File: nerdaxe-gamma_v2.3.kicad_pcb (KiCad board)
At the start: 4 copper layers, 60.8 x 99.8 mm, 130 parts, among them J1 54-00164, J6 Conn_01x04, T1 net-tie, U10 EMC2101, U11 T-Display-S3, U2 TPS546D24ARVFR, U5 MCP1824T-1202E/OT, U6 MCP1824T-0802E, U7 25MHz, U8 BM1370_mode1, U9 SN74AVC4T774

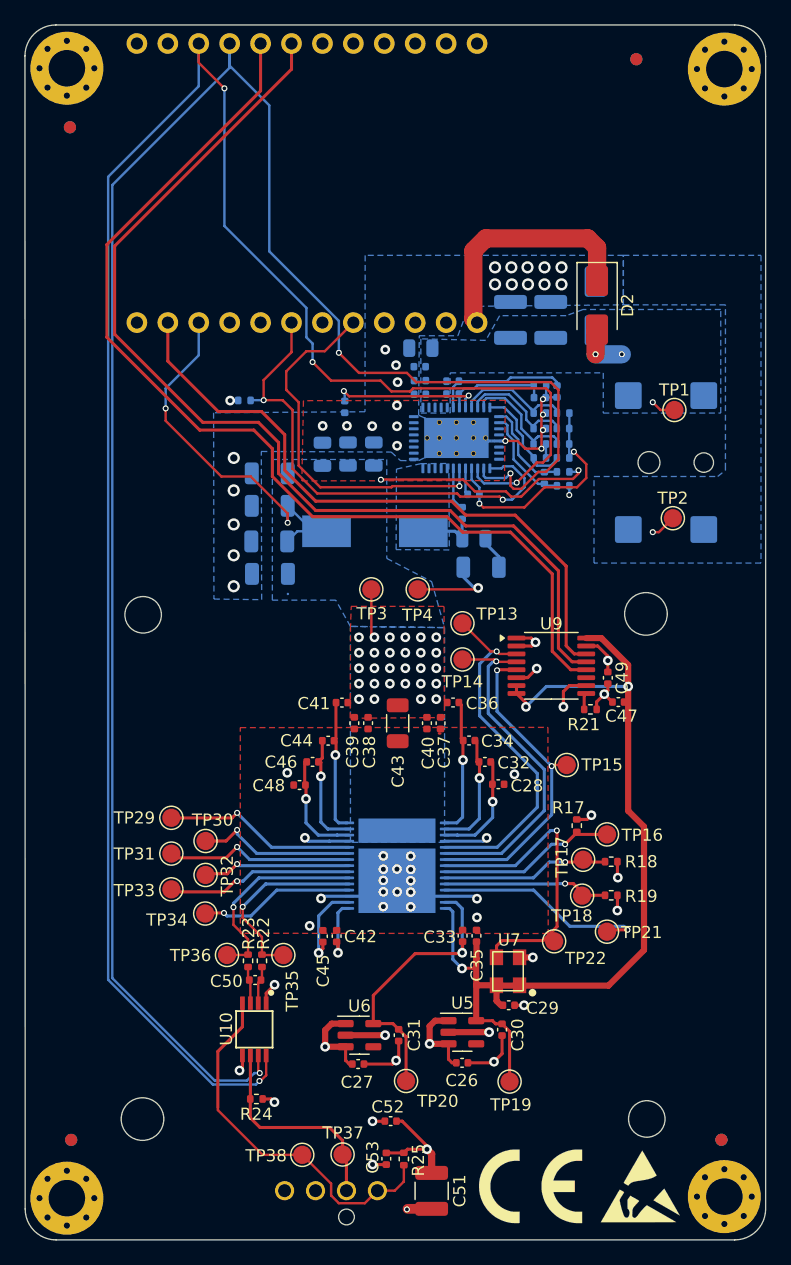
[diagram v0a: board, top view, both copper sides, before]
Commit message: Nerdaxe Gamma v2.3
- Fix Emi CE needs
- Added ferrite beads + EMI blocking capacitors
- New components added: R16, R20, R26, R27C21, C22, C23, FB1, FB2, FB3, FB4, FB5, FB6
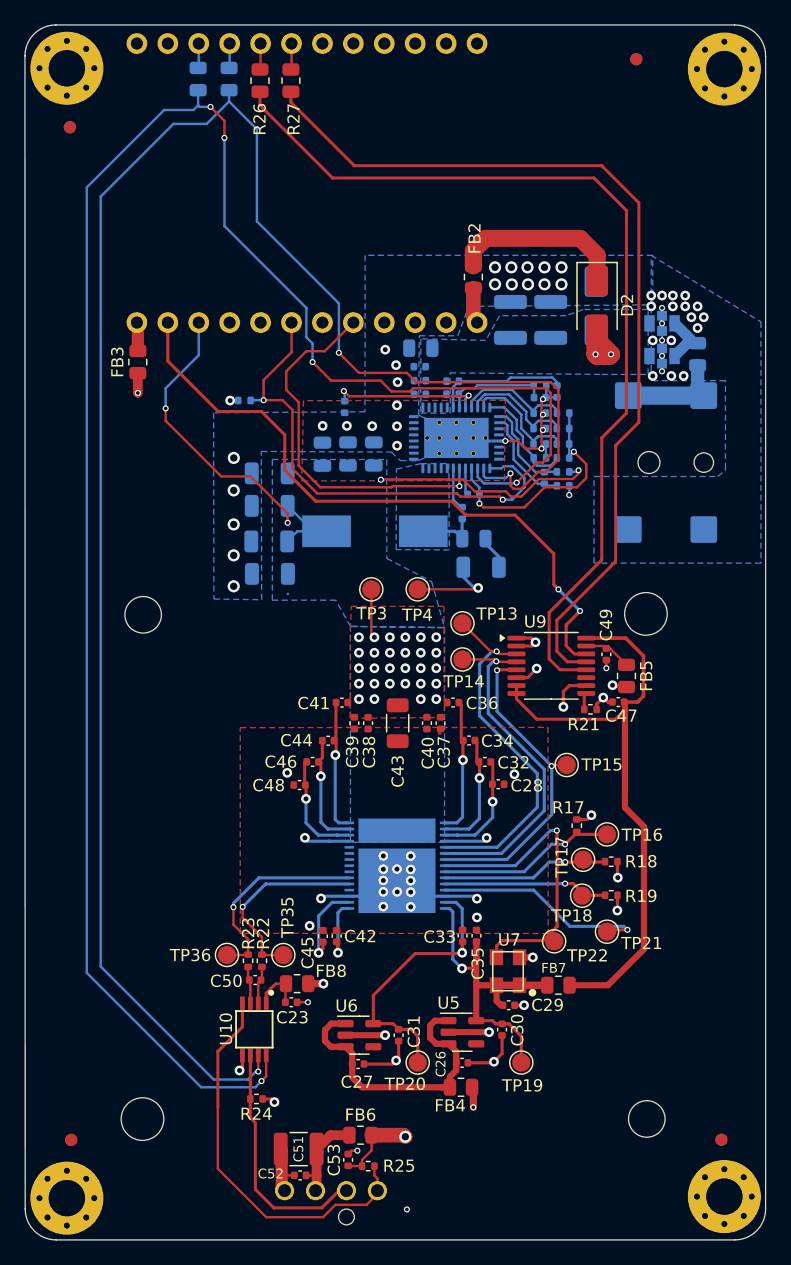
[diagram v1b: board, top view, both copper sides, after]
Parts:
- removed REF**: CE-Logo_8.5x6mm_SilkScreen, Symbol:CE-Logo_8.5x6mm_SilkScreen
- removed REF**: ESD-Logo_6.6x6mm_SilkScreen, Symbol:ESD-Logo_6.6x6mm_SilkScreen
- removed REF**: OSHW-Logo2_7.3x6mm_SilkScreen, Symbol:OSHW-Logo2_7.3x6mm_SilkScreen
- removed TP1, TP2, TP29, TP30, TP31, TP32, TP33, TP34, TP37, TP38: TestPoint, TestPoint:TestPoint_Pad_D1.5mm
- added C21: NFM21PC105B1C3D, bitaxe:NFM21PC105B1C3D_MUR, B.Cu at (127.4, 74.7)
- added C22: NFM21PC105B1C3D, bitaxe:NFM21PC105B1C3D_MUR, B.Cu at (127.4, 72.0)
- added C23: 0.1uF, Capacitor_SMD:C_0402_1005Metric, F.Cu at (96.9, 127.8)
- added FB1: 2508051217Y6, Resistor_SMD:R_0805_2012Metric, B.Cu at (130.3, 74.5)
- added FB2: MPZ2012S221A, Resistor_SMD:R_0805_2012Metric, F.Cu at (111.9, 68.2)
- added FB3: BLM21PG221SN1D, Resistor_SMD:R_0805_2012Metric, F.Cu at (84.3, 75.2)
- added FB4: BLM21PG221SN1D, Resistor_SMD:R_0805_2012Metric, F.Cu at (110.9, 134.7)
- added FB5: BLM21PG221SN1D, Resistor_SMD:R_0805_2012Metric, F.Cu at (124.5, 101.0)
- added FB6: BLM21PG221SN1D, Resistor_SMD:R_0805_2012Metric, F.Cu at (102.6, 138.7)
- added FB7: BLM21PG221SN1D, Resistor_SMD:R_0805_2012Metric, F.Cu at (118.9, 126.4)
- added FB8: BLM21PG221SN1D, Resistor_SMD:R_0805_2012Metric, F.Cu at (97.4, 126.2)
- added R16: 33, Resistor_SMD:R_0805_2012Metric, B.Cu at (89.3, 51.9)
- added R20: 33, Resistor_SMD:R_0805_2012Metric, B.Cu at (91.8, 51.9)
- added R26: 33, Resistor_SMD:R_0805_2012Metric, F.Cu at (94.4, 52.1)
- added R27: 33, Resistor_SMD:R_0805_2012Metric, F.Cu at (96.9, 52.1)
- moved C51 11.4 mm to (97.5, 139.8), turned to 180 degrees
- moved C52 8.67 mm to (97.7, 142.0)
- moved C53 3.14 mm to (101.6, 140.7), turned to 90 degrees
- moved R25 2.98 mm to (103.3, 141.2), turned to 180 degrees
- moved C49 1.94 mm to (122.8, 99.2)
- moved TP19 1.84 mm to (115.8, 132.7)
- moved TP20 1.79 mm to (107.3, 132.7)
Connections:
- C26 pad 1: /5V -> /BM1370/5Vf
- C27 pad 1: /5V -> /BM1370/5Vf
- C47 pad 1: /BM1370/1V2 -> /BM1370/1V2fb
- C49 pad 1: /3V3 -> Net-(U9-VCCB)
- C51 pad 1: /5V -> Net-(J6-Pin_2)
- C52 pad 1: /5V -> Net-(J6-Pin_2)
- J1 pad 1: /5V -> /Power/V_JACK
- J6 pad 2: /5V -> Net-(J6-Pin_2)
- U10 pad 1: /3V3 -> Net-(U10-VDD)
- U11 pad 1: /3V3 -> Net-(FB3-Pad2)
- U11 pad 12: Net-(D2-K) -> Net-(U11-5V)
- U11 pad 13: /3V3 -> unconnected-(U11-3V-Pad13)
- U11 pad 19: /TX -> Net-(U11-GPIO17)
- U11 pad 20: /RX -> Net-(U11-GPIO18)
- U11 pad 21: /SDA -> Net-(U11-GPIO44)
- U11 pad 22: /SCL -> Net-(U11-GPIO43)
- U5 pad 1: /5V -> /BM1370/5Vf
- U5 pad 3: /5V -> /BM1370/5Vf
- U6 pad 1: /5V -> /BM1370/5Vf
- U6 pad 3: /5V -> /BM1370/5Vf
- U9 pad 15: /3V3 -> Net-(U9-VCCB)
- U9 pad 16: /BM1370/1V2 -> /BM1370/1V2fb
- U9 pad 7: /BM1370/1V2 -> /BM1370/1V2fb
- U9 pad 8: /BM1370/1V2 -> /BM1370/1V2fb
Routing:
- net /3V3: track 6.96 -> 161.8 mm, vias 4 -> 5
- net /BM1370/1V2fb: track 0.00 -> 50.3 mm
- net /BM1370/1V2: track 76.7 -> 27.6 mm, vias 3 -> 1
- net /5V: track 156.6 -> 111.7 mm, vias 6 -> 4
- net /BM1370/5Vf: track 0.00 -> 25.4 mm
- net /BM1370/NRSTO: track 16.1 -> 0.00 mm, vias 1 -> 0
- net /BM1370/BO: track 15.5 -> 0.00 mm, vias 1 -> 0
- net /BM1370/RI: track 15.5 -> 0.00 mm, vias 1 -> 0
- net /BM1370/CO: track 13.2 -> 0.00 mm, vias 1 -> 0
- net /BM1370/PIN_MODE: track 12.8 -> 0.00 mm, vias 1 -> 0
- net /BM1370/CLKO: track 12.2 -> 0.00 mm, vias 1 -> 0
- net /TX: track 85.0 -> 75.2 mm
- net /Power/V_JACK: track 0.00 -> 8.89 mm
- net Net-(J6-Pin_2): track 0.00 -> 7.48 mm
- net /RX: track 85.1 -> 77.7 mm
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- added copper zone on In2.Cu, net GND
- removed copper zone on In2.Cu, net /3V3
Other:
- board text added: "rev.2.3"
- board text removed: "rev.2.1"
